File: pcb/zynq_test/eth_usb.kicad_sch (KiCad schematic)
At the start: 2 parts, among them J1001 RJ45_Hanrun_HR911105A_Horizon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, J1002 USB_A_Stacked

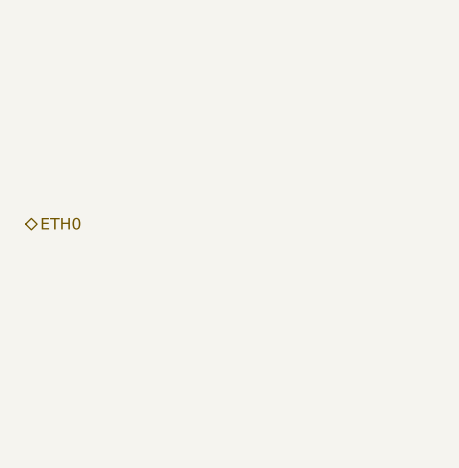
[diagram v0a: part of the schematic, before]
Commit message: Added Cameras, changed SD card IC for skew reasons
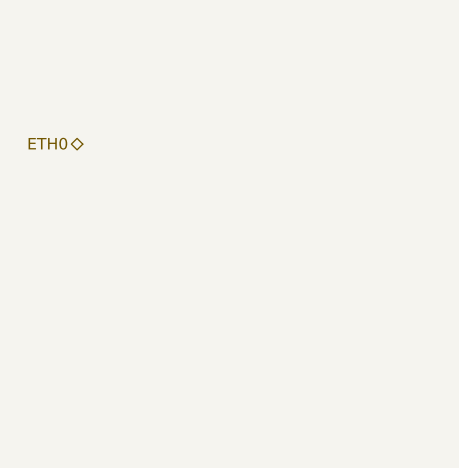
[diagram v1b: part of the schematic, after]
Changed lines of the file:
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@@
 	(hierarchical_label "ETH0"
 		(shape bidirectional)
-		(at 38.1 60.96 0)
+		(at 44.45 52.07 180)
 		(effects
 			(font
 				(size 1.27 1.27)
 			)
-			(justify left)
+			(justify right)
 		)
 	)
